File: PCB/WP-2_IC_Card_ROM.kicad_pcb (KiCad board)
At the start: 2 copper layers, 45 x 54 mm, 6 parts, among them J1 Conn_01x38_Female, U1 FLASH 256Kx8 5v Parallel, U2 FLASH 256Kx8 5v Parallel

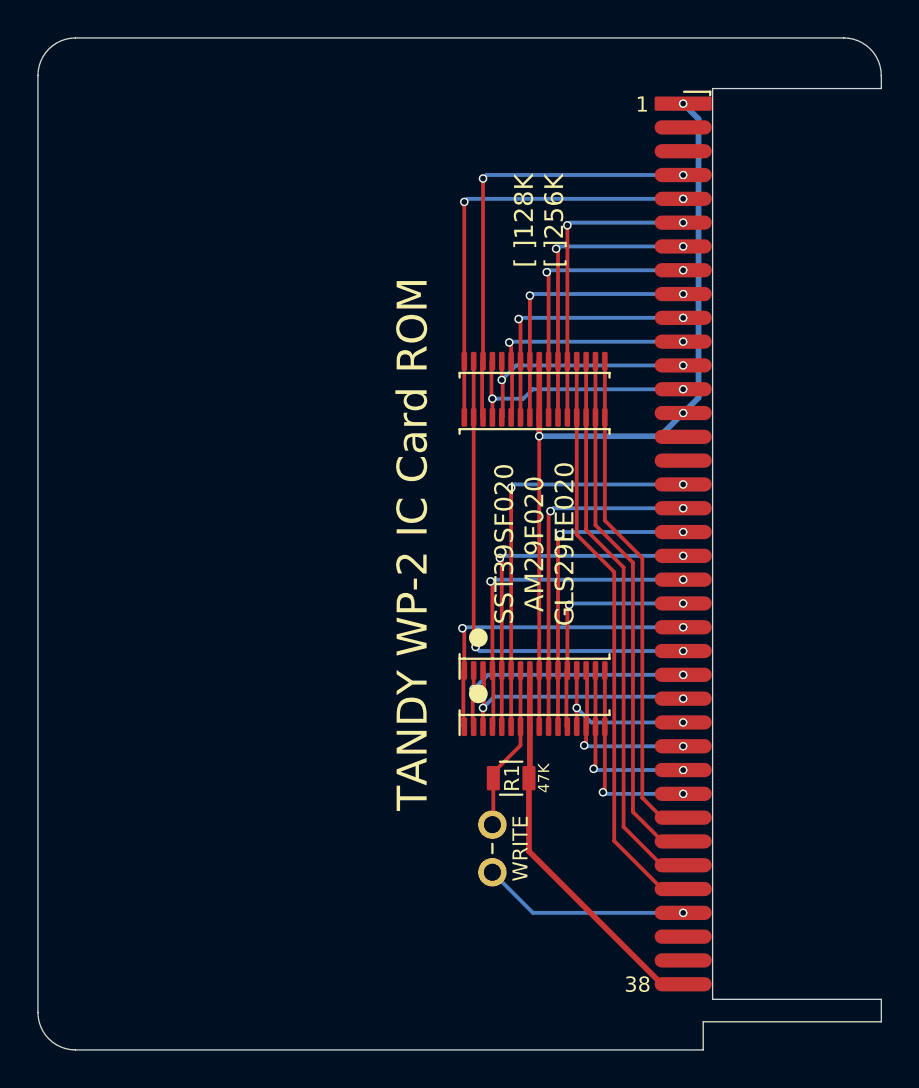
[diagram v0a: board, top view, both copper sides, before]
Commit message: more clean up from ditching the small boards
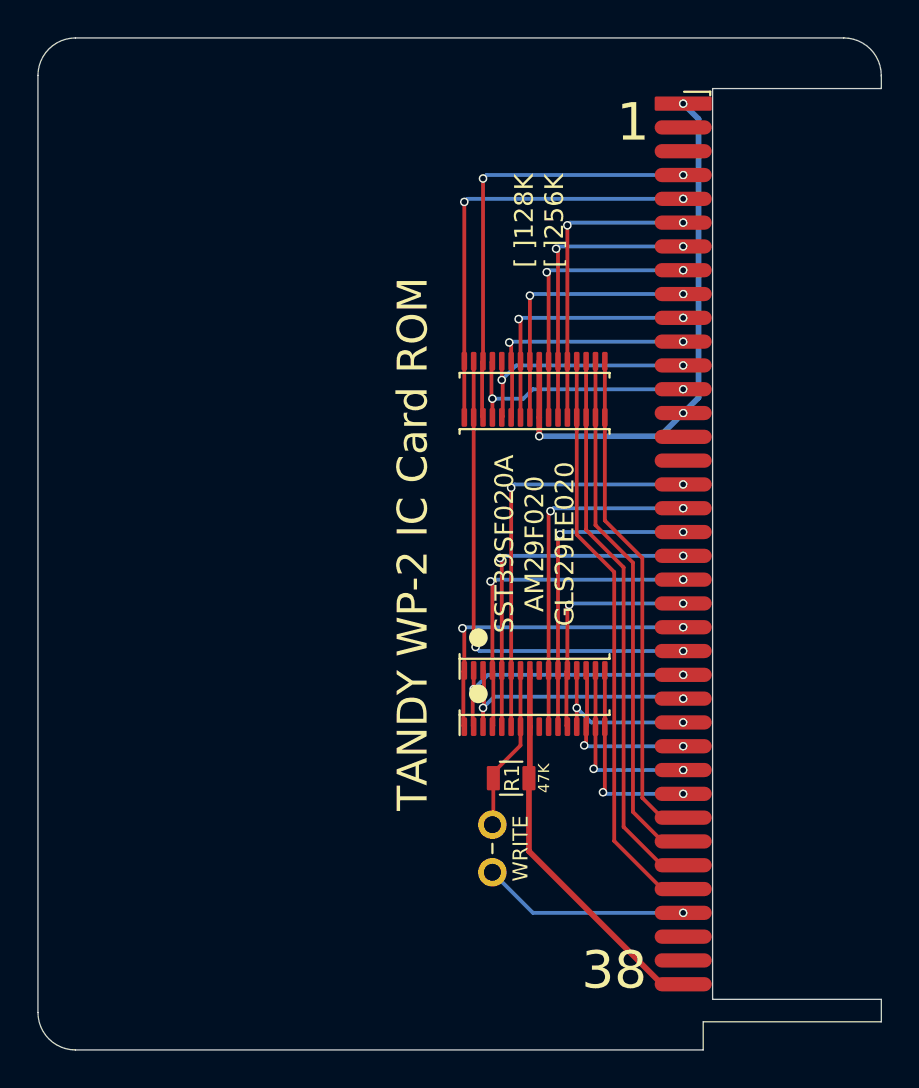
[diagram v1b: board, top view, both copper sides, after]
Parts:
- removed NT1: Net-Tie_2, 0_LOCAL:Net_Tie_2p_8mil
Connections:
- U1 pad 9: /A18 -> (no net)
- U2 pad 9: /A18 -> (no net)
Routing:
- net GND: track 40.4 -> 29.4 mm
- net /A18: track 4.05 -> 0.00 mm
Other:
- board text added: "SST39SF020A AM29F020 GLS29EE020"
- board text removed: "SST39SF020 AM29F020 GLS29EE020"

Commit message: larger 1x38 holes in prog adapt, silkscreen
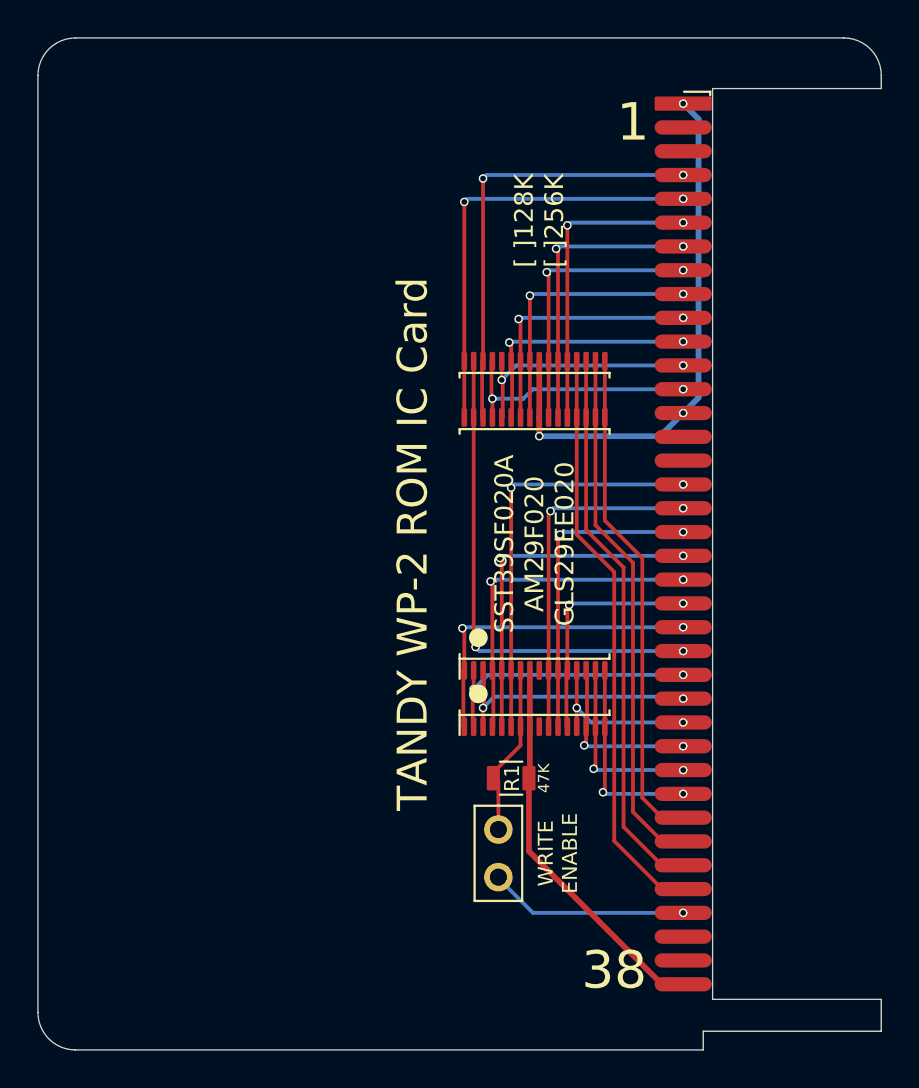
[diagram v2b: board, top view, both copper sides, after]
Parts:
- moved JP1 0.41 mm to (147.3, 116.2)
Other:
- outline, holes or cut-outs redrawn
- board text added: "TANDY WP-2 ROM IC Card"
- board text added: "WRITE ENABLE"
- board text removed: "TANDY WP-2 IC Card ROM"
- board text removed: "WRITE"

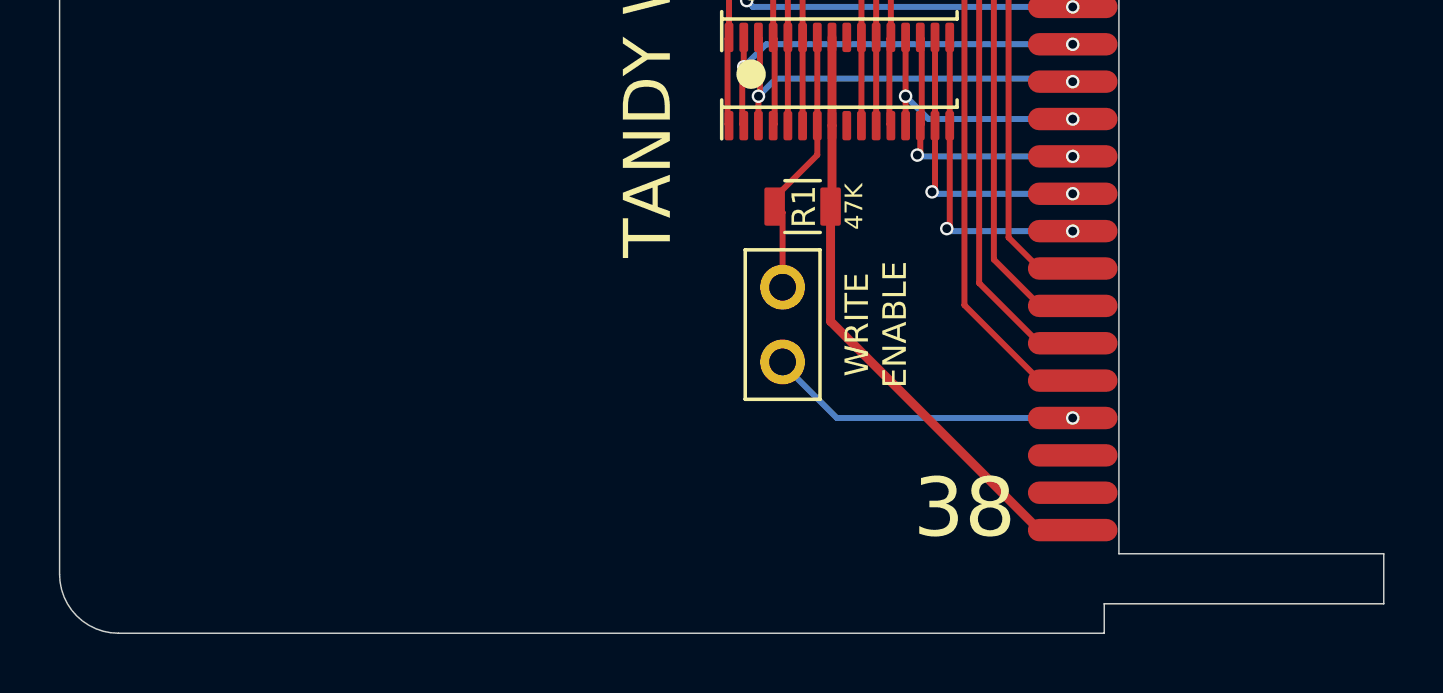
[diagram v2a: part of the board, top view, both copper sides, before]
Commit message: silkscreen board name, small board outline tweak
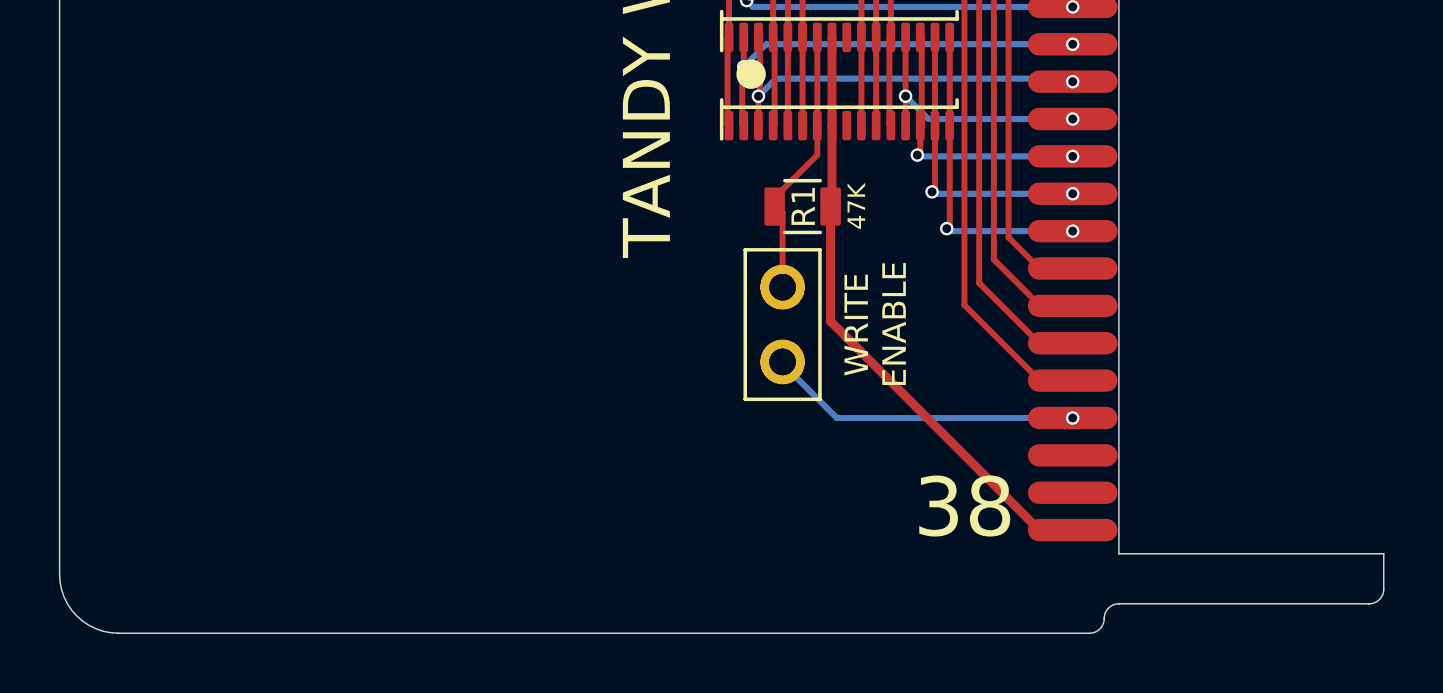
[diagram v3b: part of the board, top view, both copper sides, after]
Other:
- outline, holes or cut-outs redrawn
- board text added: "WP-2_IC_Card_ROM v002"
- board text removed: "WP-2_IC_Card_ROM_no_carrier v001"

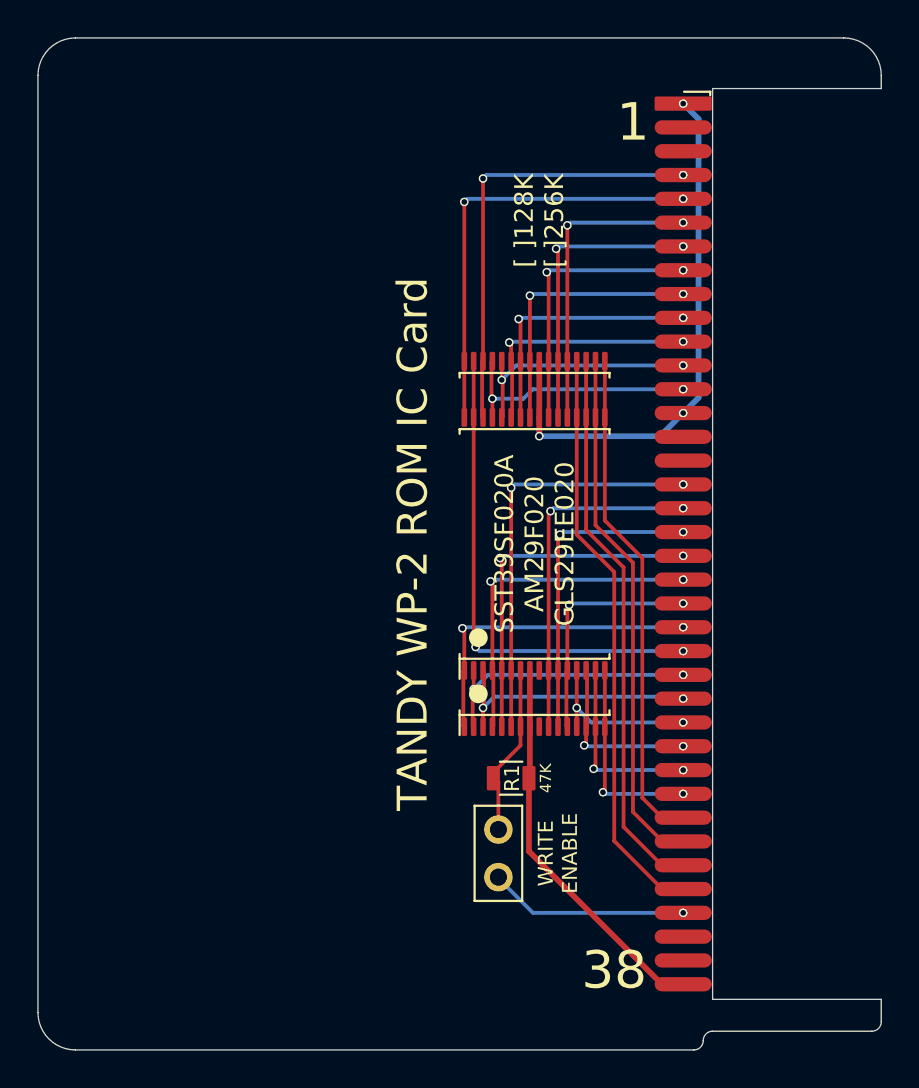
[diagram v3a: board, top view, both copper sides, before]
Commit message: v003 - edge cut finger pulls, easier diodes and batt holder for RAM
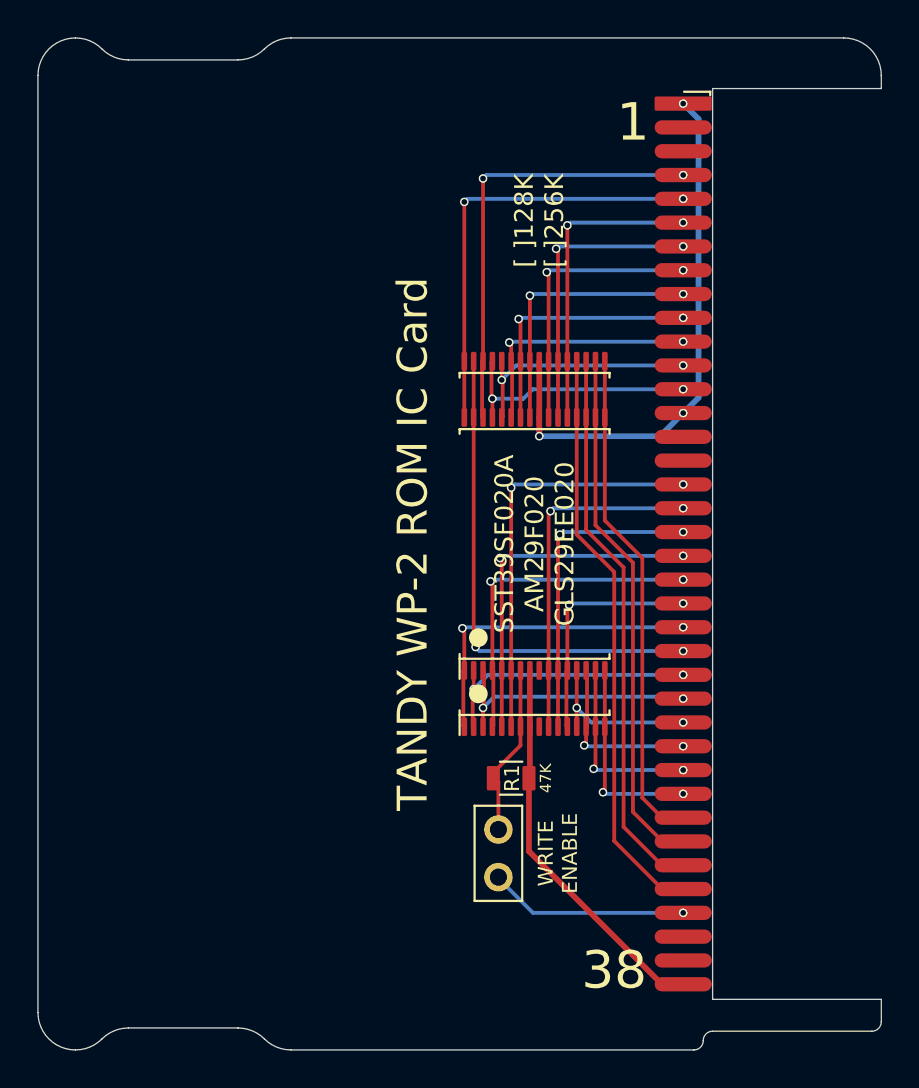
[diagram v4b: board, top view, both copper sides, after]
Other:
- outline, holes or cut-outs redrawn
- board text added: "WP-2_IC_Card_ROM v003"
- board text removed: "WP-2_IC_Card_ROM v002"
